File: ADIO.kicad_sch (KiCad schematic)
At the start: 8 parts, among them U11 BTS70xx-TBD, U12 BTS70xx-TBD, U13 BTS70xx-TBD, U14 BTS70xx-TBD, U15 BTS70xx-TBD, U16 BTS70xx-TBD, U17 BTS70xx-TBD, U18 BTS70xx-TBD

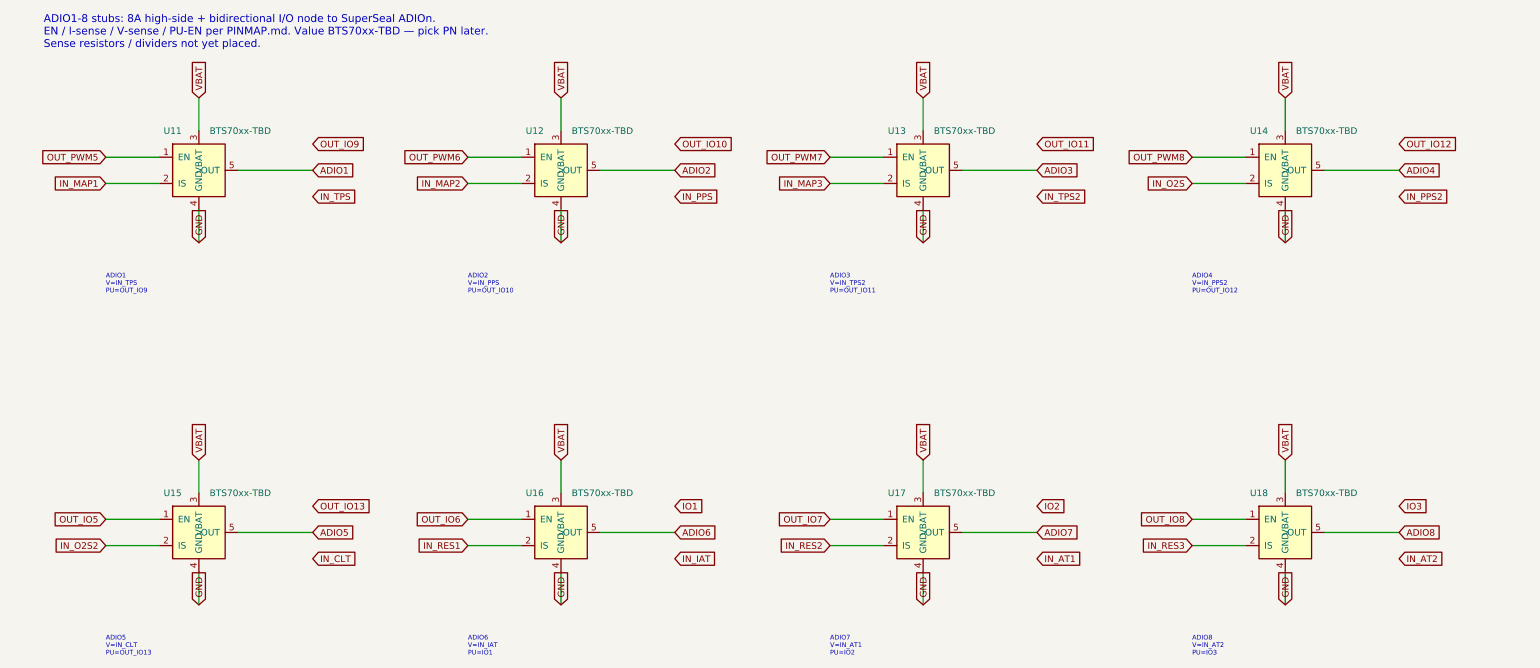
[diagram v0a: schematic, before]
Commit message: Clear fab blockers 1–4: SuperSeal 9-6437287-8, PROFET PNs, power entry, PCB place
- Replace Conn_02x13 pin-header with TE/AMP SuperSeal 1.0 26-way
  (9-6437287-8, keying 1) via pdmrazora.pretty footprint (6473423-1 pattern)
- HP: keep BTS50010-1TAD; add RIS 2k7 + 10n; fix IN/IS wiring
- ADIO: BTS7004-1EPP; RIS 4k7 + soft PU 4k7 to SENSOR_5V; fix EN/IS wiring
- Power entry: fuse/TVS/bulk stubs + IGN_SW 100k/10k (~11:1) → IN_VIGN
- PCB: place SuperSeal, HP×4, ADIO×8 with nets; outline 180×140; thermal zones
- Document PNs, kILIS, AmpsPerVolt TODOs in HARDWARE_BOM.md / BOARD.md

Do not touch HELLCORE.
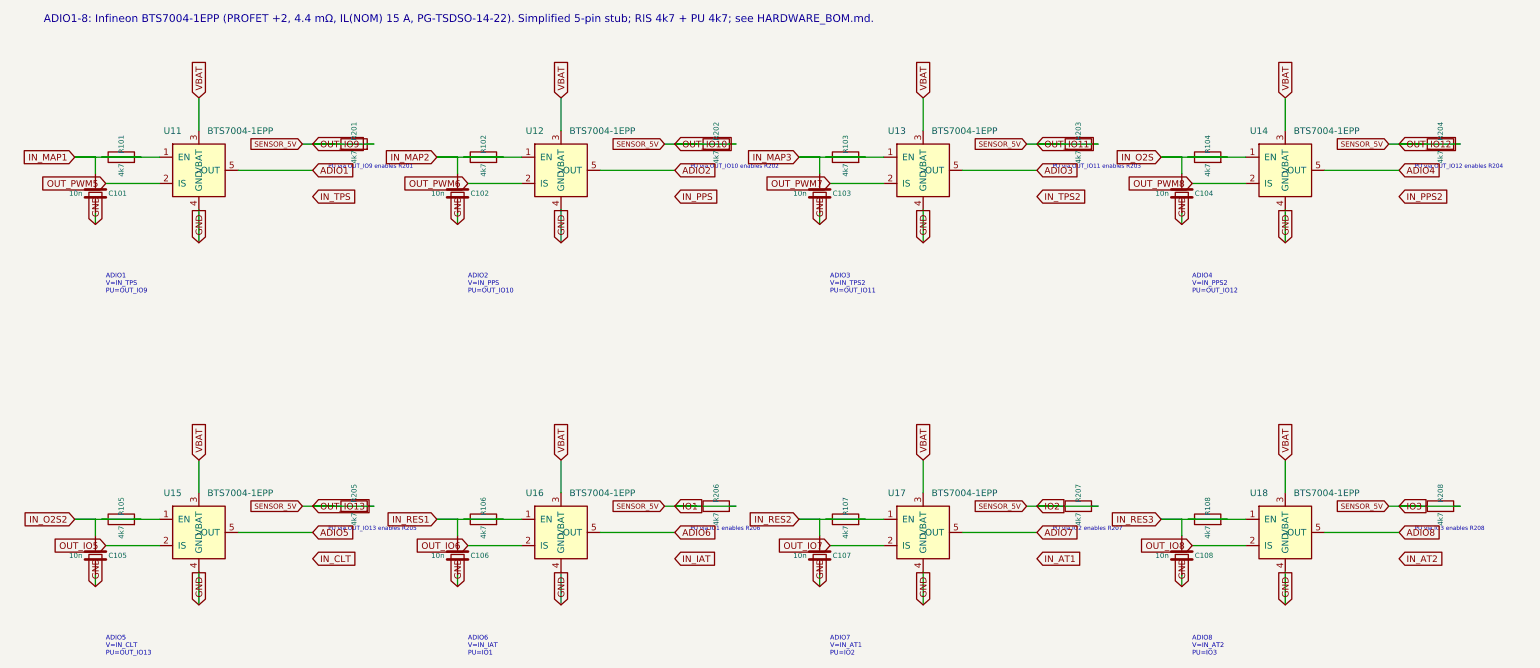
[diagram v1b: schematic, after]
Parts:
- added C101, C102, C103, C104, C105, C106, C107, C108: 10n, Capacitor_SMD:C_0603_1608Metric, symbol Device:C
- added R101, R102, R103, R104, R105, R106, R107, R108, R201, R202, R203, R204, R205, R206, R207, R208: 4k7, Resistor_SMD:R_0603_1608Metric, symbol Device:R
- U11, U12, U13, U14, U15, U16, U17, U18: value BTS70xx-TBD -> BTS7004-1EPP; footprint (none) -> Package_SO:Infineon_PG-TSDSO-14-22
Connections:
- net GND: now also C101.2, C102.2, C103.2, C104.2, C105.2, C106.2, C107.2, C108.2
- net IN_MAP1: now also U11.1 (EN), C101.1, R101.1, R101.2; no longer U11.2 (IS)
- net IN_MAP2: now also U12.1 (EN), C102.1, R102.1, R102.2; no longer U12.2 (IS)
- net IN_MAP3: now also U13.1 (EN), C103.1, R103.1, R103.2; no longer U13.2 (IS)
- net IN_O2S: now also U14.1 (EN), C104.1, R104.1, R104.2; no longer U14.2 (IS)
- net IN_O2S2: now also U15.1 (EN), C105.1, R105.1, R105.2; no longer U15.2 (IS)
- net IN_RES1: now also U16.1 (EN), C106.1, R106.1, R106.2; no longer U16.2 (IS)
- net IN_RES2: now also U17.1 (EN), C107.1, R107.1, R107.2; no longer U17.2 (IS)
- net IN_RES3: now also U18.1 (EN), C108.1, R108.1, R108.2; no longer U18.2 (IS)
- net IO1: now also R201.1, R201.2, R202.1, R202.2, R203.1, R203.2, R204.1, R204.2, R205.1, R205.2, R206.1, R206.2, R207.1, R207.2, R208.1, R208.2
- net OUT_IO5: now also U15.2 (IS); no longer U15.1 (EN)
- net OUT_IO6: now also U16.2 (IS); no longer U16.1 (EN)
- net OUT_IO7: now also U17.2 (IS); no longer U17.1 (EN)
- net OUT_IO8: now also U18.2 (IS); no longer U18.1 (EN)
- net OUT_PWM5: now also U11.2 (IS); no longer U11.1 (EN)
- net OUT_PWM6: now also U12.2 (IS); no longer U12.1 (EN)
- net OUT_PWM7: now also U13.2 (IS); no longer U13.1 (EN)
- net OUT_PWM8: now also U14.2 (IS); no longer U14.1 (EN)
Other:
- note added: "ADIO1-8: Infineon BTS7004-1EPP (PROFET +2, 4.4 mΩ, IL(NOM) 15 A, PG-TSDSO-14-22). Simplified 5-pin stub; RIS 4k7 + PU 4k7; see HARDWARE_BOM.md."
- note added: "PU via IO1 enables R206"
- note added: "PU via IO2 enables R207"
- note added: "PU via IO3 enables R208"
- note added: "PU via OUT_IO10 enables R202"
- note added: "PU via OUT_IO11 enables R203"
- note added: "PU via OUT_IO12 enables R204"
- note added: "PU via OUT_IO13 enables R205"
- note added: "PU via OUT_IO9 enables R201"
- note removed: "ADIO1-8 stubs: 8A high-side + bidirectional I/O node to SuperSeal ADIOn. EN / I-sense / V-sense / PU-EN per PINMAP.md. Value BTS70xx-TBD — pick PN later. Sense resistors / dividers not yet placed."
